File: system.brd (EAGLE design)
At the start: 55.9 x 82.5 mm, 127 parts, among them IC1 TPS7B8650BQDDARQ1, J1 OLED, J2 163-179PH-EX, J4 MCU, U1 ATMEGA328PB-AU, Y1 ABL-16.000MHZ-B2

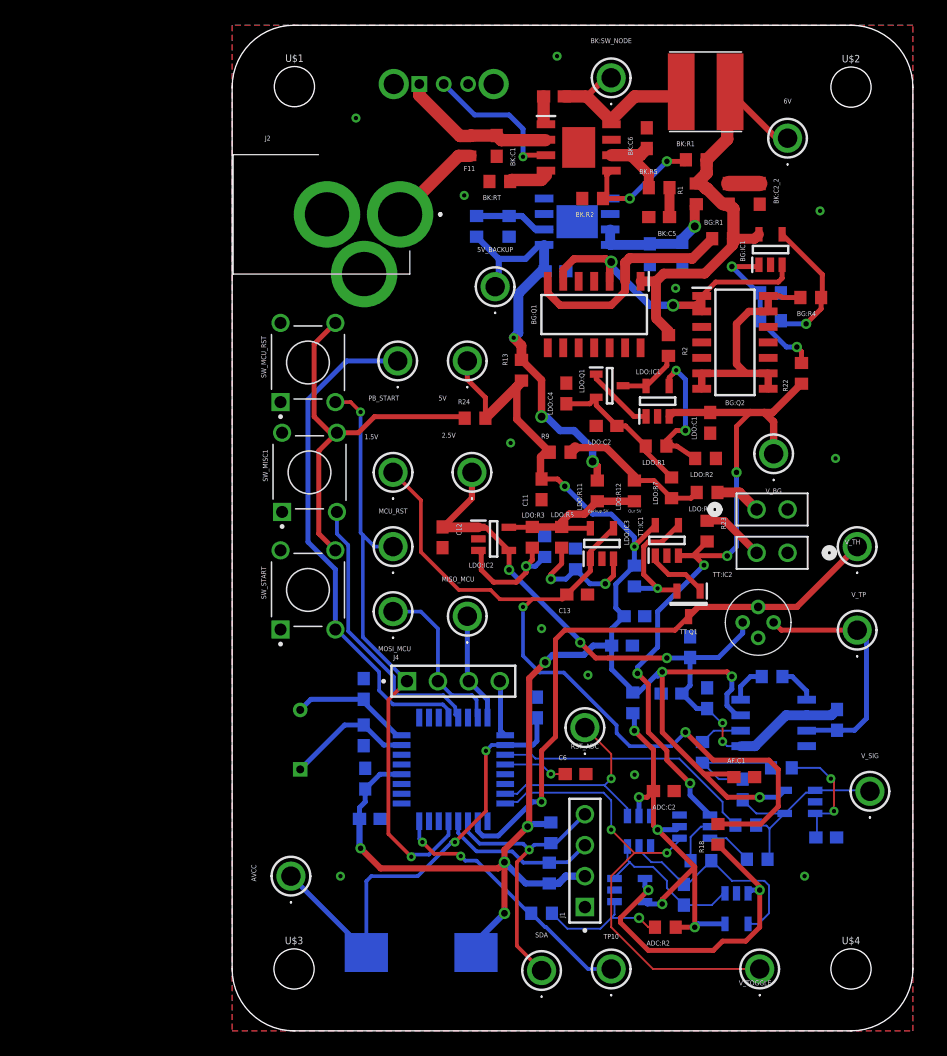
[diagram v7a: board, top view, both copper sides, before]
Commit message: fixed airwire errors
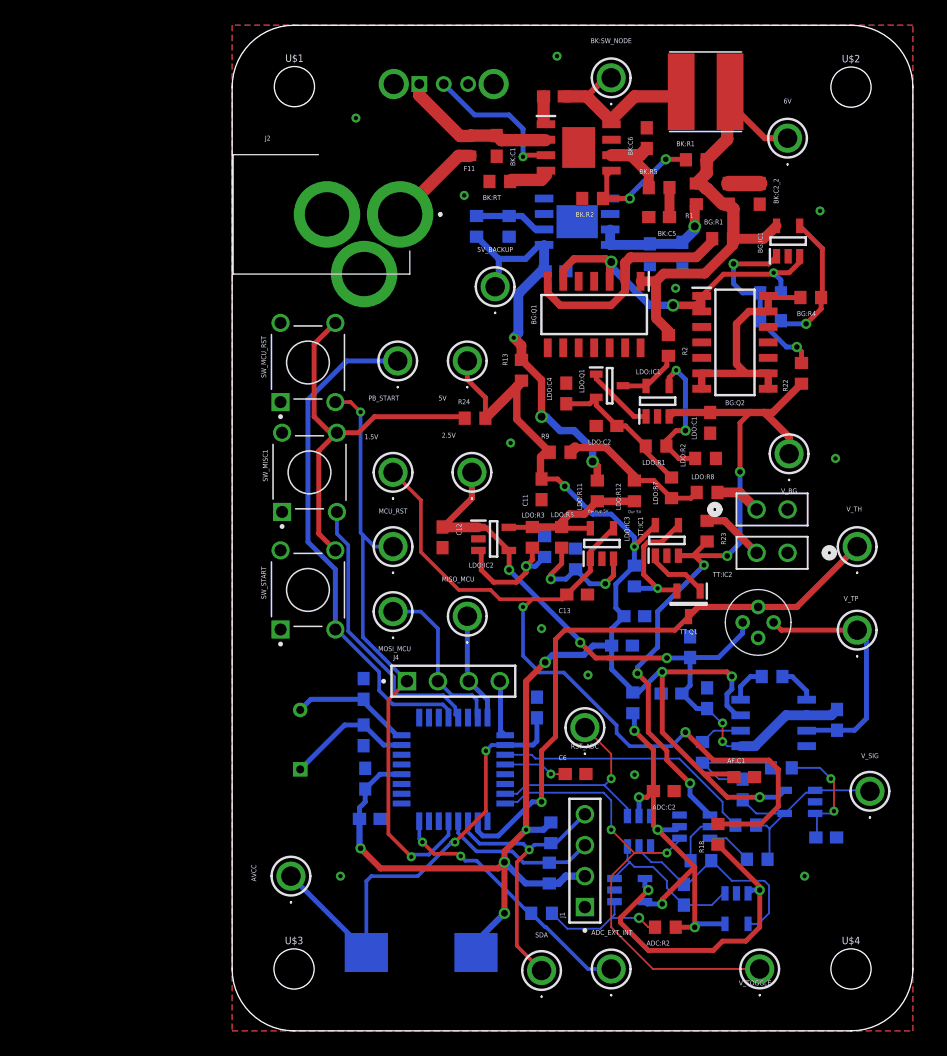
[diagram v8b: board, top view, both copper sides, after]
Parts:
- moved BG:IC1 1.60 mm to (43.1, 52.1)
- moved V_BG 1.27 mm to (43.2, 34.7)
- renumbered TP10 to ADC_EXT_INT
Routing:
- net VS_6V: track 36.0 -> 39.4 mm
- net BG:N$2: track 26.9 -> 30.1 mm, vias 2 -> 3
- net N$7: track 13.2 -> 15.6 mm
- net VS_5V_OUT: track 144.3 -> 142.2 mm
- net LDO:LS_5V: track 14.8 -> 13.9 mm
- net N$10: track 6.64 -> 6.00 mm
- net LDO:N$1: track 12.6 -> 11.9 mm
- net V_BG: track 62.2 -> 62.7 mm
